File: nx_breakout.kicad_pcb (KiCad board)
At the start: 2 copper layers, 24.1 x 56.5 mm, 19 parts, among them J1 Conn_02x20_Odd_Even, J2 Conn_01x06, J3 Conn_01x04, J4 Conn_01x04, J5 Conn_01x04_Male, U1 SN74LVC1G14DBV, U2 SN74LVC1G14DBV, U3 SN74LVC1G14DBV, U4 SN74LVC1G14DBV, U5 SN74LVC1G14DBV

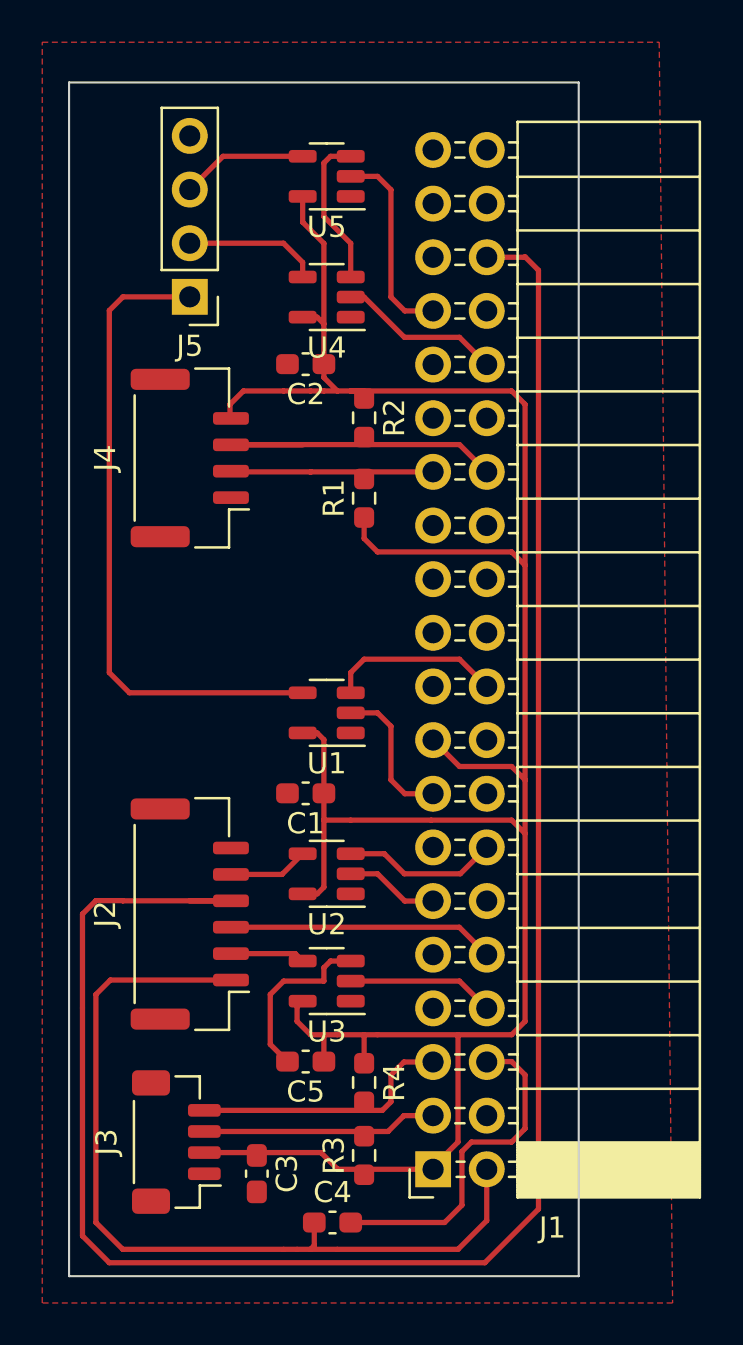
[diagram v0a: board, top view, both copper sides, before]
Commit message: Add files via upload
Corrected to non-inverting Schmitt triggers.
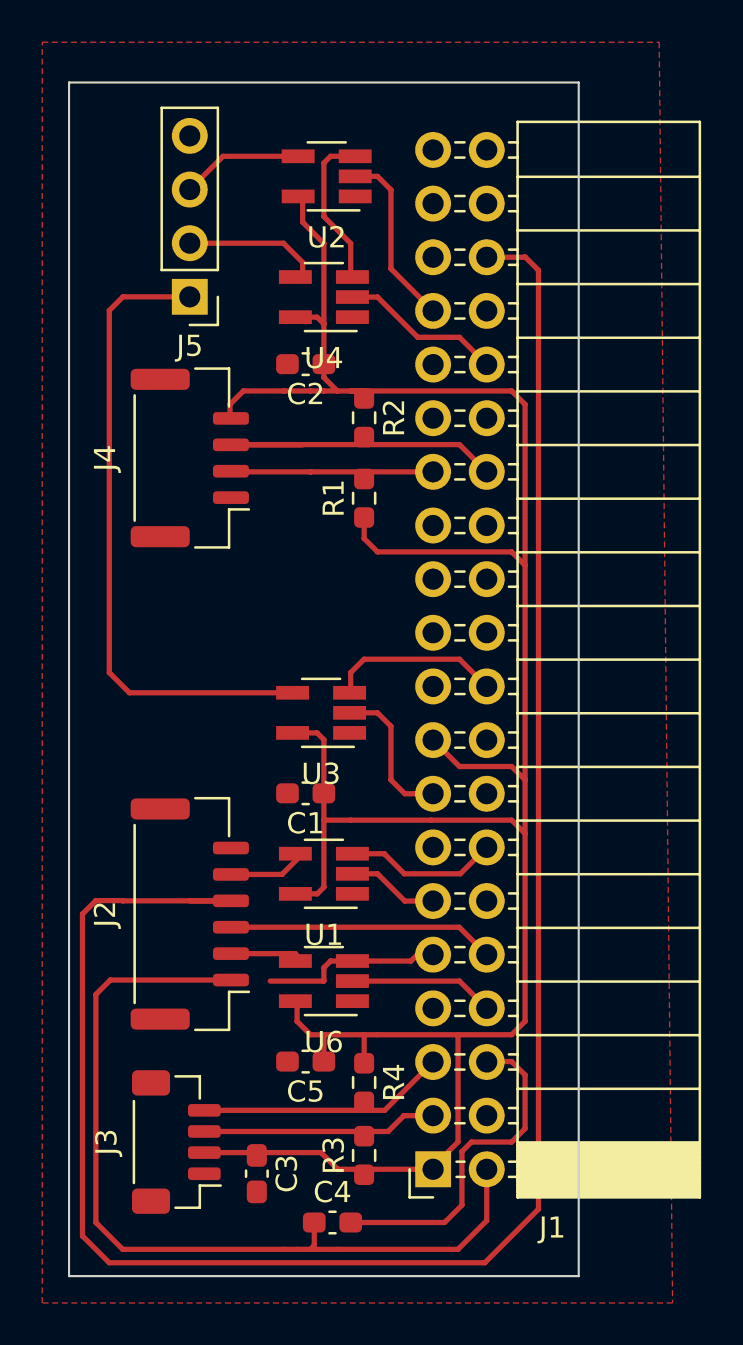
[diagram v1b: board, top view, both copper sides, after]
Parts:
- removed U5: SN74LVC1G14DBV, Package_TO_SOT_SMD:SOT-23-5
- added U6: 74LVC1G17, Package_TO_SOT_SMD:SOT-23-5_HandSoldering, F.Cu at (127.0, 113.0)
- U1, U2, U3, U4: value SN74LVC1G14DBV -> 74LVC1G17; footprint Package_TO_SOT_SMD:SOT-23-5 -> Package_TO_SOT_SMD:SOT-23-5_HandSoldering
- moved U2 33.0 mm to (127.1, 74.9)
- moved U3 12.7 mm to (126.9, 100.3)
- moved U1 7.62 mm to (127.0, 108.0)
- moved U4 0.13 mm to (127.0, 80.6)
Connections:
- J2 pad 2: Net-(J2-Pad2) -> Net-(U6-Pad4)
- U1 pad 1: unconnected-(U1-Pad1) -> (no net)
- U1 pad 2: /GPIO12 -> /UART1_RTS
- U1 pad 4: Net-(J5-Pad1) -> Net-(J2-Pad5)
- U2 pad 1: unconnected-(U2-Pad1) -> (no net)
- U2 pad 2: /UART1_RTS -> /GPIO13
- U2 pad 4: Net-(J2-Pad5) -> Net-(J5-Pad3)
- U3 pad 1: unconnected-(U3-Pad1) -> (no net)
- U3 pad 2: /UART1_TX -> /GPIO12
- U3 pad 4: Net-(J2-Pad2) -> Net-(J5-Pad1)
- U4 pad 1: unconnected-(U4-Pad1) -> (no net)
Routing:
- net Net-(U6-Pad4): track 0.00 -> 3.54 mm
- net Net-(J2-Pad2): track 3.54 -> 0.00 mm
- net /GPIO13: track 9.51 -> 8.73 mm
- net /I2C1_SCL: track 12.5 -> 11.8 mm
- net GND: track 47.4 -> 48.0 mm
- net /GPIO07: track 7.76 -> 8.32 mm
